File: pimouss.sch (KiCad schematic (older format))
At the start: 20 parts

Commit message: sch: Add misc doc texts
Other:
- note added: "Extension connector\n"
- note added: "JTAG connector"
- moved on the sheet: J?, P?C
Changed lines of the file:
@@
 L pimouss-motherboard:QSH-060-01-L-D-A P?
 U 3 1 5CE77EA3
-P 9800 2250
-F 0 "P?" H 10000 2437 60  0000 C CNN
-F 1 "QSH-060-01-L-D-A" H 10000 2331 60  0000 C CNN
-F 2 "pimouss-motherboard:QSH-060-01-L-D-A" V 10100 -350 39  0001 C CNN
-F 3 "" H 10000 1550 60  0001 C CNN
-F 4 "Samtec" H 10000 -150 39  0001 C CNN "Manufacturer"
-	3    9800 2250
+P 9700 3450
+F 0 "P?" H 9900 3637 60  0000 C CNN
+F 1 "QSH-060-01-L-D-A" H 9900 3531 60  0000 C CNN
+F 2 "pimouss-motherboard:QSH-060-01-L-D-A" V 10000 850 39  0001 C CNN
+F 3 "" H 9900 2750 60  0001 C CNN
+F 4 "Samtec" H 9900 1050 39  0001 C CNN "Manufacturer"
+	3    9700 3450
 	1    0    0    -1
 $EndComp
@@
 L power:GND #PWR?
 U 1 1 5CE7813B
-P 9600 2750
-F 0 "#PWR?" H 9600 2500 50  0001 C CNN
-F 1 "GND" H 9605 2577 50  0000 C CNN
-F 2 "" H 9600 2750 50  0001 C CNN
-F 3 "" H 9600 2750 50  0001 C CNN
-	1    9600 2750
+P 9500 3950
+F 0 "#PWR?" H 9500 3700 50  0001 C CNN
+F 1 "GND" H 9505 3777 50  0000 C CNN
+F 2 "" H 9500 3950 50  0001 C CNN
+F 3 "" H 9500 3950 50  0001 C CNN
+	1    9500 3950
 	1    0    0    -1
 $EndComp
@@
 L power:GND #PWR?
 U 1 1 5CE7816A
-P 10400 2750
-F 0 "#PWR?" H 10400 2500 50  0001 C CNN
-F 1 "GND" H 10405 2577 50  0000 C CNN
-F 2 "" H 10400 2750 50  0001 C CNN
-F 3 "" H 10400 2750 50  0001 C CNN
-	1    10400 2750
-	1    0    0    -1
-$EndComp
-Wire Wire Line
-	10300 2350 10400 2350
-Wire Wire Line
-	10400 2350 10400 2450
-Wire Wire Line
-	10300 2450 10400 2450
-Connection ~ 10400 2450
-Wire Wire Line
-	10400 2450 10400 2550
-Wire Wire Line
-	10300 2550 10400 2550
-Connection ~ 10400 2550
-Wire Wire Line
-	10400 2550 10400 2650
-Wire Wire Line
-	10300 2650 10400 2650
-Connection ~ 10400 2650
-Wire Wire Line
-	10400 2650 10400 2750
-Wire Wire Line
-	9700 2350 9600 2350
-Wire Wire Line
-	9600 2350 9600 2450
-Wire Wire Line
-	9700 2450 9600 2450
-Connection ~ 9600 2450
-Wire Wire Line
-	9600 2450 9600 2550
-Wire Wire Line
-	9600 2550 9700 2550
-Connection ~ 9600 2550
-Wire Wire Line
-	9600 2550 9600 2650
-Wire Wire Line
-	9700 2650 9600 2650
-Connection ~ 9600 2650
-Wire Wire Line
-	9600 2650 9600 2750
+P 10300 3950
+F 0 "#PWR?" H 10300 3700 50  0001 C CNN
+F 1 "GND" H 10305 3777 50  0000 C CNN
+F 2 "" H 10300 3950 50  0001 C CNN
+F 3 "" H 10300 3950 50  0001 C CNN
+	1    10300 3950
+	1    0    0    -1
+$EndComp
+Wire Wire Line
+	10200 3550 10300 3550
+Wire Wire Line
+	10300 3550 10300 3650
+Wire Wire Line
+	10200 3650 10300 3650
+Connection ~ 10300 3650
+Wire Wire Line
+	10300 3650 10300 3750
+Wire Wire Line
+	10200 3750 10300 3750
+Connection ~ 10300 3750
+Wire Wire Line
+	10300 3750 10300 3850
+Wire Wire Line
+	10200 3850 10300 3850
+Connection ~ 10300 3850
+Wire Wire Line
+	10300 3850 10300 3950
+Wire Wire Line
+	9600 3550 9500 3550
+Wire Wire Line
+	9500 3550 9500 3650
+Wire Wire Line
+	9600 3650 9500 3650
+Connection ~ 9500 3650
+Wire Wire Line
+	9500 3650 9500 3750
+Wire Wire Line
+	9500 3750 9600 3750
+Connection ~ 9500 3750
+Wire Wire Line
+	9500 3750 9500 3850
+Wire Wire Line
+	9600 3850 9500 3850
+Connection ~ 9500 3850
+Wire Wire Line
+	9500 3850 9500 3950
 Wire Wire Line
 	2300 1600 2200 1600
@@
 L pimouss-motherboard:TMS-105-57-GD J?
 U 1 1 5DAB4506
-P 9350 900
-F 0 "J?" H 9450 1067 50  0000 C CNN
-F 1 "TMS-105-57-GD" H 9450 976 50  0000 C CNN
-F 2 "pimouss-motherboard:TMS-105-57-G-D" H 9350 800 50  0001 C CNN
-F 3 "~" H 9400 700 50  0001 C CNN
-	1    9350 900
+P 9800 2050
+F 0 "J?" H 9900 2217 50  0000 C CNN
+F 1 "TMS-105-57-GD" H 9900 2126 50  0000 C CNN
+F 2 "pimouss-motherboard:TMS-105-57-G-D" H 9800 1950 50  0001 C CNN
+F 3 "~" H 9850 1850 50  0001 C CNN
+	1    9800 2050
 	1    0    0    -1
 $EndComp
@@
 L power:+5V #PWR?
 U 1 1 5DAB4C7D
-P 9000 900
-F 0 "#PWR?" H 9000 750 50  0001 C CNN
-F 1 "+5V" H 9015 1073 50  0000 C CNN
-F 2 "" H 9000 900 50  0001 C CNN
-F 3 "" H 9000 900 50  0001 C CNN
-	1    9000 900
+P 9450 2050
+F 0 "#PWR?" H 9450 1900 50  0001 C CNN
+F 1 "+5V" H 9465 2223 50  0000 C CNN
+F 2 "" H 9450 2050 50  0001 C CNN
+F 3 "" H 9450 2050 50  0001 C CNN
+	1    9450 2050
 	1    0    0    -1
 $EndComp
@@
 L power:GND #PWR?
 U 1 1 5DAB4CAB
-P 9900 1400
-F 0 "#PWR?" H 9900 1150 50  0001 C CNN
-F 1 "GND" H 9905 1227 50  0000 C CNN
-F 2 "" H 9900 1400 50  0001 C CNN
-F 3 "" H 9900 1400 50  0001 C CNN
-	1    9900 1400
-	1    0    0    -1
-$EndComp
-Wire Wire Line
-	9000 900  9000 1000
-Wire Wire Line
-	9000 1300 9200 1300
-Wire Wire Line
-	9000 1200 9200 1200
-Connection ~ 9000 1200
-Wire Wire Line
-	9000 1200 9000 1300
-Wire Wire Line
-	9000 1100 9200 1100
-Connection ~ 9000 1100
-Wire Wire Line
-	9000 1100 9000 1200
-Wire Wire Line
-	9000 1000 9200 1000
-Connection ~ 9000 1000
-Wire Wire Line
-	9000 1000 9000 1100
-Wire Wire Line
-	9700 1000 9900 1000
-Wire Wire Line
-	9900 1000 9900 1100
-Wire Wire Line
-	9700 1100 9900 1100
-Connection ~ 9900 1100
-Wire Wire Line
-	9900 1100 9900 1200
-Wire Wire Line
-	9700 1200 9900 1200
-Connection ~ 9900 1200
-Wire Wire Line
-	9900 1200 9900 1300
-Wire Wire Line
-	9700 1300 9900 1300
-Connection ~ 9900 1300
-Wire Wire Line
-	9900 1300 9900 1400
-Text Notes 9950 1800 2    50   ~ 0
+P 10350 2550
+F 0 "#PWR?" H 10350 2300 50  0001 C CNN
+F 1 "GND" H 10355 2377 50  0000 C CNN
+F 2 "" H 10350 2550 50  0001 C CNN
+F 3 "" H 10350 2550 50  0001 C CNN
+	1    10350 2550
+	1    0    0    -1
+$EndComp
+Wire Wire Line
+	9450 2050 9450 2150
+Wire Wire Line
+	9450 2450 9650 2450
+Wire Wire Line
+	9450 2350 9650 2350
+Connection ~ 9450 2350
+Wire Wire Line
+	9450 2350 9450 2450
+Wire Wire Line
+	9450 2250 9650 2250
+Connection ~ 9450 2250
+Wire Wire Line
+	9450 2250 9450 2350
+Wire Wire Line
+	9450 2150 9650 2150
+Connection ~ 9450 2150
+Wire Wire Line
+	9450 2150 9450 2250
+Wire Wire Line
+	10150 2150 10350 2150
+Wire Wire Line
+	10350 2150 10350 2250
+Wire Wire Line
+	10150 2250 10350 2250
+Connection ~ 10350 2250
+Wire Wire Line
+	10350 2250 10350 2350
+Wire Wire Line
+	10150 2350 10350 2350
+Connection ~ 10350 2350
+Wire Wire Line
+	10350 2350 10350 2450
+Wire Wire Line
+	10150 2450 10350 2450
+Connection ~ 10350 2450
+Wire Wire Line
+	10350 2450 10350 2550
+Text Notes 10400 2950 2    50   ~ 0
 Pimouss SoM power connector
 Text Notes 4200 6850 0    50   ~ 0
@@
 Wire Bus Line
 	5350 2400 5350 4300
+Text Notes 9700 6400 0    50   ~ 0
+JTAG connector
+Text Notes 7000 6400 0    50   ~ 0
+Extension connector\n
 $EndSCHEMATC

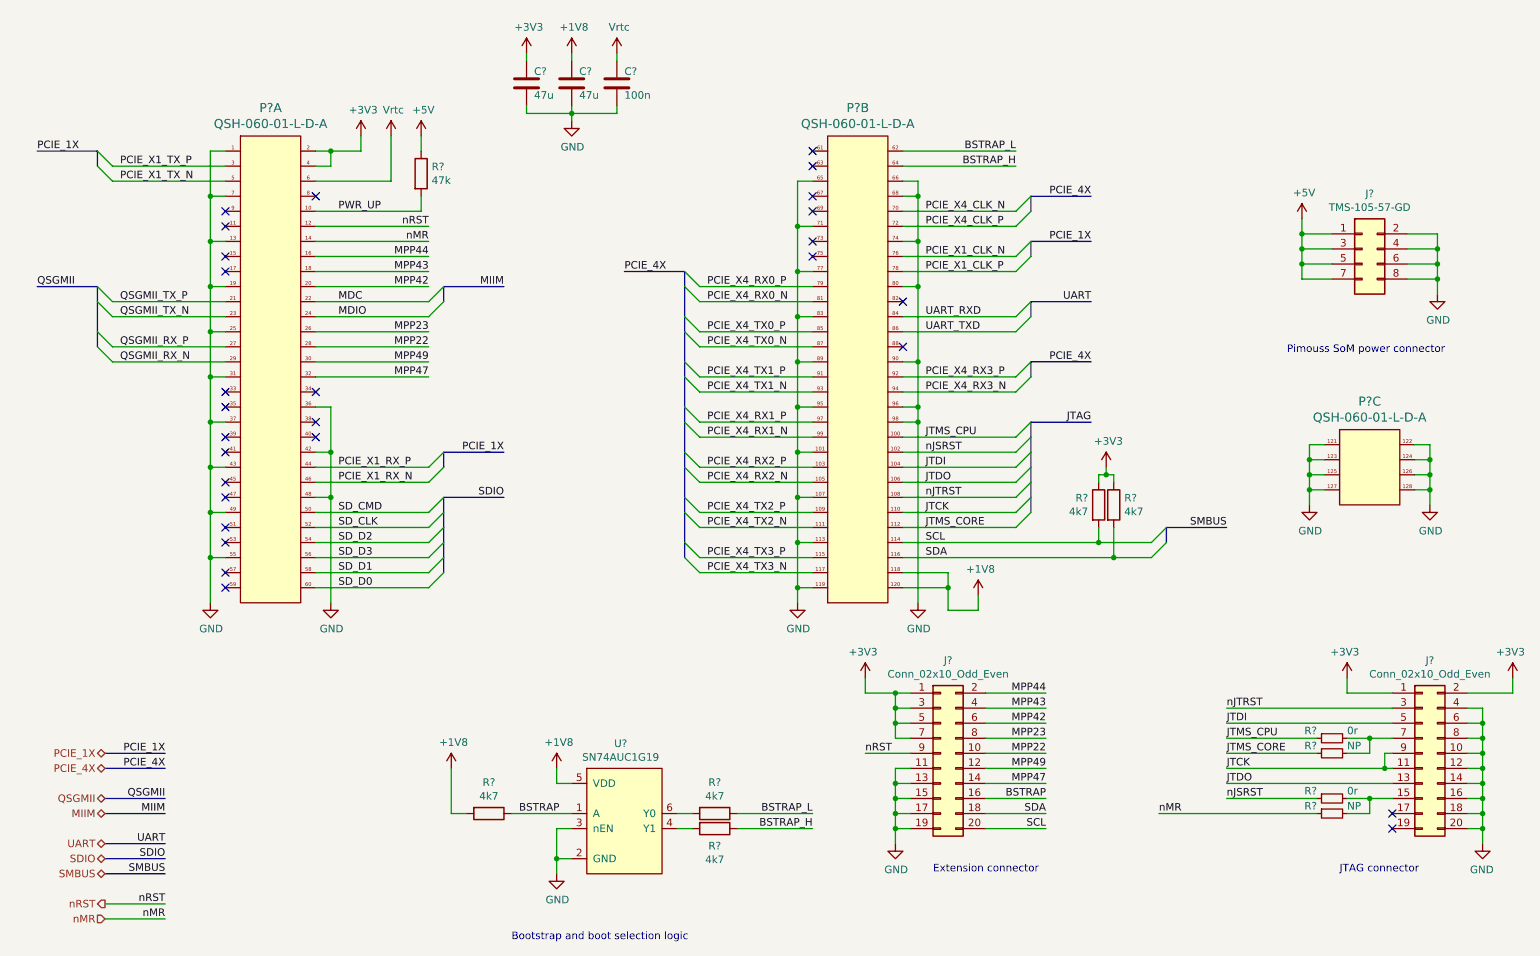
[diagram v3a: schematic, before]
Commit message: sch: Replace regular symbols with small variant
Done for most capacitors and resistors
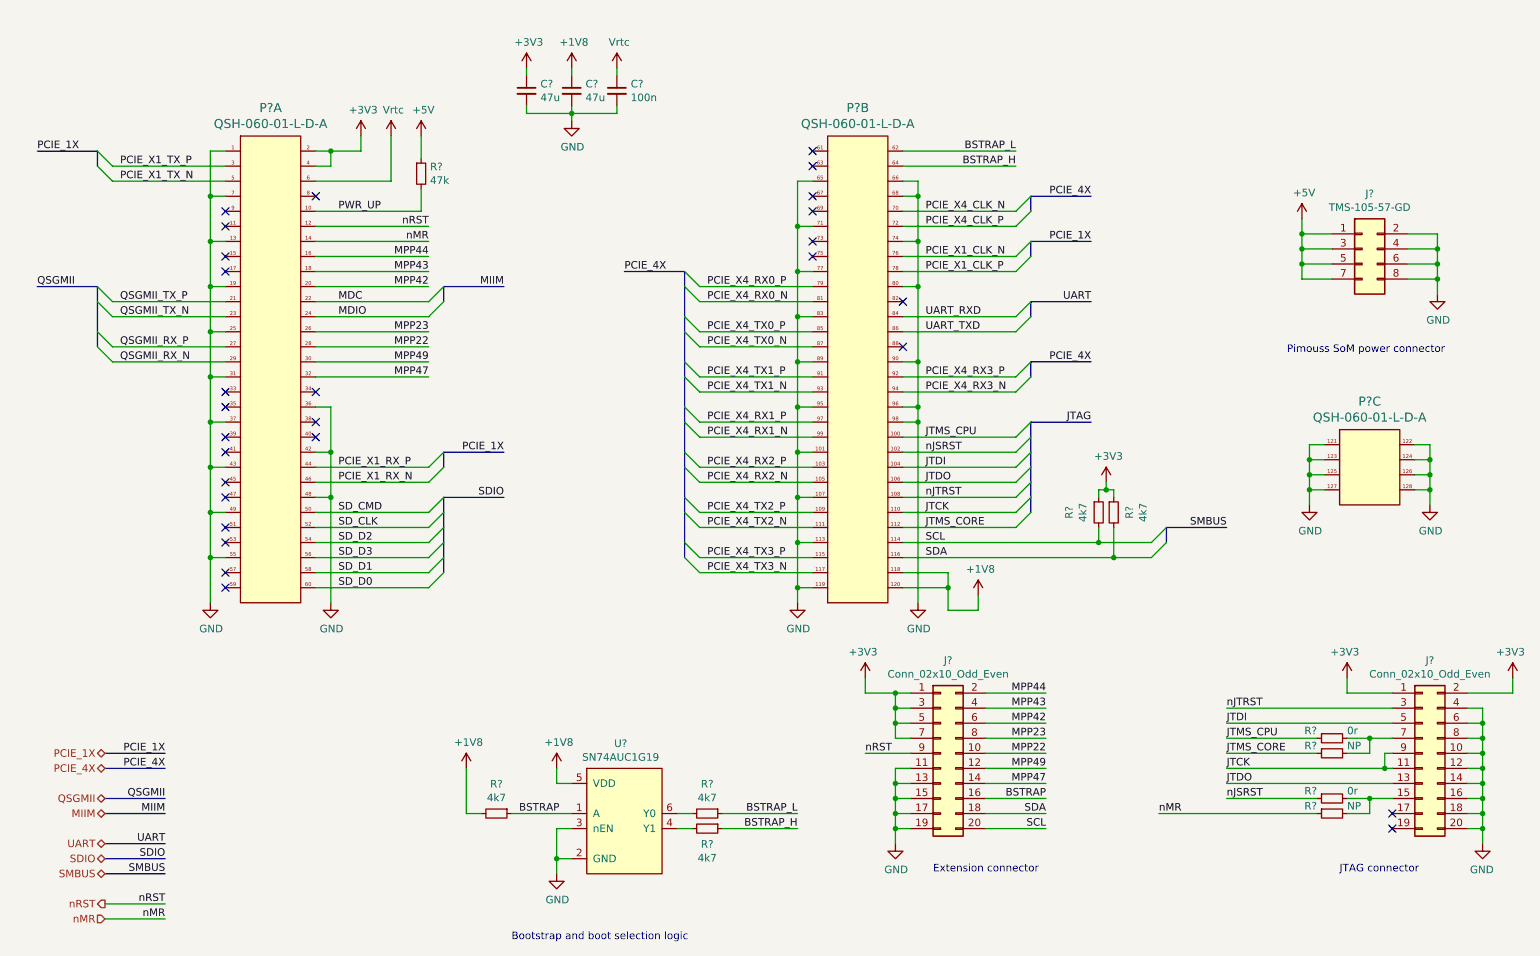
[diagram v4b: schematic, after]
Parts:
- removed C? (x2): 47u, symbol Device:C
- removed C?: 100n, symbol Device:C
- removed R? (x5): 4k7, symbol Device:R
- removed R?: 47k, symbol Device:R
- added C? (x2): 47u, symbol Device:C_Small
- added C?: 100n, symbol Device:C_Small
- added R?: 47k, symbol Device:R_Small
- added R? (x5): 4k7, symbol Device:R_Small
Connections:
- net +1V8: now also C?.1, R?.2
- net +3V3: now also C?.1, R?.1, R?.1
- net +5V: now also R?.1
- net BSTRAP: now also R?.1
- net BSTRAP_H: now also R?.1
- net BSTRAP_L: now also R?.1
- net GND: now also C?.2, C?.2, C?.2
- net PWR_UP: now also R?.2
- net SCL: now also R?.2
- net SDA: now also R?.2
- net Vrtc: now also C?.1
- net at U?.4 (Y1): now also R?.2
- net at U?.6 (Y0): now also R?.2
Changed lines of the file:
@@
 	1    0    0    -1
 $EndComp
-$Comp
-L Device:R R?
-U 1 1 5CF0D15E
-P 8100 3950
-F 0 "R?" H 8030 3996 50  0000 R CNN
-F 1 "4k7" H 8030 3905 50  0000 R CNN
-F 2 "" V 8030 3950 50  0001 C CNN
-F 3 "~" H 8100 3950 50  0001 C CNN
-	1    8100 3950
-	1    0    0    -1
-$EndComp
-Wire Wire Line
-	3600 1500 3600 1600
-Wire Wire Line
-	3600 2000 3600 1900
+Wire Wire Line
+	3600 1500 3600 1650
+Wire Wire Line
+	3600 2000 3600 1850
 Wire Wire Line
 	2900 2000 3600 2000
@@
 nMR
 $Comp
-L Device:C C?
-U 1 1 5D16D02B
-P 4300 1150
-F 0 "C?" H 4350 1200 50  0000 L BNN
-F 1 "47u" H 4350 1100 50  0000 L TNN
-F 2 "" H 4338 1000 50  0001 C CNN
-F 3 "~" H 4300 1150 50  0001 C CNN
-	1    4300 1150
-	1    0    0    -1
-$EndComp
-$Comp
-L Device:C C?
-U 1 1 5D16D167
-P 4600 1150
-F 0 "C?" H 4650 1200 50  0000 L BNN
-F 1 "47u" H 4650 1100 50  0000 L TNN
-F 2 "" H 4638 1000 50  0001 C CNN
-F 3 "~" H 4600 1150 50  0001 C CNN
-	1    4600 1150
-	1    0    0    -1
-$EndComp
-$Comp
-L Device:C C?
-U 1 1 5D16D193
-P 4900 1150
-F 0 "C?" H 4950 1200 50  0000 L BNN
-F 1 "100n" H 4950 1100 50  0000 L TNN
-F 2 "" H 4938 1000 50  0001 C CNN
-F 3 "~" H 4900 1150 50  0001 C CNN
-	1    4900 1150
-	1    0    0    -1
-$EndComp
-$Comp
 L power:+3V3 #PWR?
 U 1 1 5D16D1F9
-P 4300 950
-F 0 "#PWR?" H 4300 800 50  0001 C CNN
-F 1 "+3V3" H 4315 1123 50  0000 C CNN
-F 2 "" H 4300 950 50  0001 C CNN
-F 3 "" H 4300 950 50  0001 C CNN
-	1    4300 950
+P 4300 1050
+F 0 "#PWR?" H 4300 900 50  0001 C CNN
+F 1 "+3V3" H 4315 1223 50  0000 C CNN
+F 2 "" H 4300 1050 50  0001 C CNN
+F 3 "" H 4300 1050 50  0001 C CNN
+	1    4300 1050
 	1    0    0    -1
 $EndComp
@@
 L power:+1V8 #PWR?
 U 1 1 5D16D346
-P 4600 950
-F 0 "#PWR?" H 4600 800 50  0001 C CNN
-F 1 "+1V8" H 4615 1123 50  0000 C CNN
-F 2 "" H 4600 950 50  0001 C CNN
-F 3 "" H 4600 950 50  0001 C CNN
-	1    4600 950
+P 4600 1050
+F 0 "#PWR?" H 4600 900 50  0001 C CNN
+F 1 "+1V8" H 4615 1223 50  0000 C CNN
+F 2 "" H 4600 1050 50  0001 C CNN
+F 3 "" H 4600 1050 50  0001 C CNN
+	1    4600 1050
 	1    0    0    -1
 $EndComp
@@
 L pimouss-motherboard:Vrtc #PWR?
 U 1 1 5D16D39E
-P 4900 950
-F 0 "#PWR?" H 4900 800 50  0001 C CNN
-F 1 "Vrtc" H 4915 1123 50  0000 C CNN
-F 2 "" H 4900 950 50  0001 C CNN
-F 3 "" H 4900 950 50  0001 C CNN
-	1    4900 950
+P 4900 1050
+F 0 "#PWR?" H 4900 900 50  0001 C CNN
+F 1 "Vrtc" H 4915 1223 50  0000 C CNN
+F 2 "" H 4900 1050 50  0001 C CNN
+F 3 "" H 4900 1050 50  0001 C CNN
+	1    4900 1050
 	1    0    0    -1
 $EndComp
@@
 $EndComp
 Wire Wire Line
-	4300 950  4300 1000
-Wire Wire Line
-	4600 950  4600 1000
-Wire Wire Line
-	4900 950  4900 1000
+	4300 1050 4300 1100
+Wire Wire Line
+	4600 1050 4600 1100
+Wire Wire Line
+	4900 1050 4900 1100
 Wire Wire Line
 	4300 1300 4300 1350
@@
 BSTRAP
 $Comp
-L Device:R R?
-U 1 1 5D1F16F9
-P 4050 6000
-F 0 "R?" V 3843 6000 50  0000 C CNN
-F 1 "4k7" V 3934 6000 50  0000 C CNN
-F 2 "" V 3980 6000 50  0001 C CNN
-F 3 "~" H 4050 6000 50  0001 C CNN
-	1    4050 6000
-	0    1    1    0
-$EndComp
-$Comp
 L power:+1V8 #PWR?
 U 1 1 5D1F18E2
-P 3800 5700
-F 0 "#PWR?" H 3800 5550 50  0001 C CNN
-F 1 "+1V8" H 3815 5873 50  0000 C CNN
-F 2 "" H 3800 5700 50  0001 C CNN
-F 3 "" H 3800 5700 50  0001 C CNN
-	1    3800 5700
-	1    0    0    -1
-$EndComp
-Wire Wire Line
-	3800 5700 3800 6000
-Wire Wire Line
-	3800 6000 3900 6000
-$Comp
-L Device:R R?
-U 1 1 5D1FB39B
-P 5550 6000
-F 0 "R?" V 5343 6000 50  0000 C CNN
-F 1 "4k7" V 5434 6000 50  0000 C CNN
-F 2 "" V 5480 6000 50  0001 C CNN
-F 3 "~" H 5550 6000 50  0001 C CNN
-	1    5550 6000
-	0    1    1    0
-$EndComp
-$Comp
-L Device:R R?
-U 1 1 5D1FB3F5
-P 5550 6100
-F 0 "R?" V 5665 6100 50  0000 C CNN
-F 1 "4k7" V 5756 6100 50  0000 C CNN
-F 2 "" V 5480 6100 50  0001 C CNN
-F 3 "~" H 5550 6100 50  0001 C CNN
-	1    5550 6100
-	0    1    1    0
-$EndComp
+P 3900 5700
+F 0 "#PWR?" H 3900 5550 50  0001 C CNN
+F 1 "+1V8" H 3915 5873 50  0000 C CNN
+F 2 "" H 3900 5700 50  0001 C CNN
+F 3 "" H 3900 5700 50  0001 C CNN
+	1    3900 5700
+	1    0    0    -1
+$EndComp
+Wire Wire Line
+	3900 5700 3900 6000
+Wire Wire Line
+	3900 6000 4000 6000
 Wire Wire Line
 	5300 6000 5400 6000
@@
 	5300 6100 5400 6100
 Wire Wire Line
-	6200 6000 5700 6000
-Wire Wire Line
-	6200 6100 5700 6100
-Text Label 6200 6000 2    50   ~ 0
+	6100 6000 5600 6000
+Wire Wire Line
+	6100 6100 5600 6100
+Text Label 6100 6000 2    50   ~ 0
 BSTRAP_L
-Text Label 6200 6100 2    50   ~ 0
+Text Label 6100 6100 2    50   ~ 0
 BSTRAP_H
 Wire Wire Line
@@
 	7100 4650 7300 4650
 Connection ~ 7100 4500
-$Comp
-L Device:R R?
-U 1 1 5CC9AC67
-P 8200 3950
-F 0 "R?" H 8270 3996 50  0000 L CNN
-F 1 "4k7" H 8270 3905 50  0000 L CNN
-F 2 "" V 8130 3950 50  0001 C CNN
-F 3 "~" H 8200 3950 50  0001 C CNN
-	1    8200 3950
-	1    0    0    -1
-$EndComp
 Wire Wire Line
 	8100 4100 8100 4200
@@
 	8200 4300 6800 4300
 Wire Wire Line
-	8100 3800 8100 3750
-Wire Wire Line
-	8100 3750 8150 3750
-Wire Wire Line
-	8200 3750 8200 3800
-$Comp
-L Device:R R?
-U 1 1 5CCB9F1D
-P 3600 1750
-F 0 "R?" H 3670 1796 50  0000 L CNN
-F 1 "47k" H 3670 1705 50  0000 L CNN
-F 2 "" V 3530 1750 50  0001 C CNN
-F 3 "~" H 3600 1750 50  0001 C CNN
-	1    3600 1750
-	1    0    0    -1
-$EndComp
+	8100 3900 8100 3850
+Wire Wire Line
+	8100 3850 8150 3850
+Wire Wire Line
+	8200 3850 8200 3900
 $Comp
 L power:+3V3 #PWR?
 U 1 1 5CCBA231
-P 8150 3700
-F 0 "#PWR?" H 8150 3550 50  0001 C CNN
-F 1 "+3V3" H 8165 3873 50  0000 C CNN
-F 2 "" H 8150 3700 50  0001 C CNN
-F 3 "" H 8150 3700 50  0001 C CNN
-	1    8150 3700
-	1    0    0    -1
-$EndComp
-Wire Wire Line
-	8150 3700 8150 3750
-Connection ~ 8150 3750
-Wire Wire Line
-	8150 3750 8200 3750
+P 8150 3800
+F 0 "#PWR?" H 8150 3650 50  0001 C CNN
+F 1 "+3V3" H 8165 3973 50  0000 C CNN
+F 2 "" H 8150 3800 50  0001 C CNN
+F 3 "" H 8150 3800 50  0001 C CNN
+	1    8150 3800
+	1    0    0    -1
+$EndComp
+Wire Wire Line
+	8150 3800 8150 3850
+Connection ~ 8150 3850
+Wire Wire Line
+	8150 3850 8200 3850
 Entry Wire Line
 	3650 4500 3750 4400
@@
 Text Notes 7000 6400 0    50   ~ 0
 Extension connector\n
+$Comp
+L Device:R_Small R?
+U 1 1 5D29A2DD
+P 3600 1750
+F 0 "R?" H 3659 1796 50  0000 L CNN
+F 1 "47k" H 3659 1705 50  0000 L CNN
+F 2 "" H 3600 1750 50  0001 C CNN
+F 3 "~" H 3600 1750 50  0001 C CNN
+	1    3600 1750
+	1    0    0    -1
+$EndComp
+$Comp
+L Device:R_Small R?
+U 1 1 5D304549
+P 4100 6000
+F 0 "R?" V 3904 6000 50  0000 C CNN
+F 1 "4k7" V 3995 6000 50  0000 C CNN
+F 2 "" H 4100 6000 50  0001 C CNN
+F 3 "~" H 4100 6000 50  0001 C CNN
+	1    4100 6000
+	0    1    1    0
+$EndComp
+$Comp
+L Device:R_Small R?
+U 1 1 5D36C2BC
+P 5500 6000
+F 0 "R?" V 5304 6000 50  0000 C CNN
+F 1 "4k7" V 5395 6000 50  0000 C CNN
+F 2 "" H 5500 6000 50  0001 C CNN
+F 3 "~" H 5500 6000 50  0001 C CNN
+	1    5500 6000
+	0    1    1    0
+$EndComp
+$Comp
+L Device:R_Small R?
+U 1 1 5D36CC4A
+P 5500 6100
+F 0 "R?" V 5604 6100 50  0000 C CNN
+F 1 "4k7" V 5695 6100 50  0000 C CNN
+F 2 "" H 5500 6100 50  0001 C CNN
+F 3 "~" H 5500 6100 50  0001 C CNN
+	1    5500 6100
+	0    1    1    0
+$EndComp
+$Comp
+L Device:R_Small R?
+U 1 1 5D3AA715
+P 8100 4000
+F 0 "R?" V 7904 4000 50  0000 C CNN
+F 1 "4k7" V 7995 4000 50  0000 C CNN
+F 2 "" H 8100 4000 50  0001 C CNN
+F 3 "~" H 8100 4000 50  0001 C CNN
+	1    8100 4000
+	1    0    0    -1
+$EndComp
+$Comp
+L Device:R_Small R?
+U 1 1 5D3AA71B
+P 8200 4000
+F 0 "R?" V 8304 4000 50  0000 C CNN
+F 1 "4k7" V 8395 4000 50  0000 C CNN
+F 2 "" H 8200 4000 50  0001 C CNN
+F 3 "~" H 8200 4000 50  0001 C CNN
+	1    8200 4000
+	1    0    0    -1
+$EndComp
+$Comp
+L Device:C_Small C?
+U 1 1 5D3D46B0
+P 4300 1200
+F 0 "C?" H 4392 1246 50  0000 L CNN
+F 1 "47u" H 4392 1155 50  0000 L CNN
+F 2 "" H 4300 1200 50  0001 C CNN
+F 3 "~" H 4300 1200 50  0001 C CNN
+	1    4300 1200
+	1    0    0    -1
+$EndComp
+$Comp
+L Device:C_Small C?
+U 1 1 5D3D4FC6
+P 4600 1200
+F 0 "C?" H 4692 1246 50  0000 L CNN
+F 1 "47u" H 4692 1155 50  0000 L CNN
+F 2 "" H 4600 1200 50  0001 C CNN
+F 3 "~" H 4600 1200 50  0001 C CNN
+	1    4600 1200
+	1    0    0    -1
+$EndComp
+$Comp
+L Device:C_Small C?
+U 1 1 5D3E9608
+P 4900 1200
+F 0 "C?" H 4992 1246 50  0000 L CNN
+F 1 "100n" H 4992 1155 50  0000 L CNN
+F 2 "" H 4900 1200 50  0001 C CNN
+F 3 "~" H 4900 1200 50  0001 C CNN
+	1    4900 1200
+	1    0    0    -1
+$EndComp
 Wire Bus Line
 	1450 2500 1450 2900
